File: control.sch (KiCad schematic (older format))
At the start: 3 parts, among them J4 ArduinoProMini

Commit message: Fix labels and lay resistors flat.
Left inputs to the line driver were backwards, because the datasheet had
an error. I think I "fixed"it before to match the datasheet.

I also decided to lay the resistors flat. They don't take up that much
room flat, and they will be easier to make pretty on the board, and more
stable with all the vibration.

Also updated the BOM and netlist.
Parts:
- R3: footprint Resistors_THT:R_Axial_DIN0204_L3.6mm_D1.6mm_P1.90mm_Vertical -> Resistors_THT:R_Axial_DIN0204_L3.6mm_D1.6mm_P5.08mm_Horizontal
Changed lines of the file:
@@
 F 0 "R3" V 4730 3400 50  0000 C CNN
 F 1 "330" V 4650 3400 50  0000 C CNN
-F 2 "Resistors_THT:R_Axial_DIN0204_L3.6mm_D1.6mm_P1.90mm_Vertical" V 4580 3400 50  0001 C CNN
+F 2 "Resistors_THT:R_Axial_DIN0204_L3.6mm_D1.6mm_P5.08mm_Horizontal" V 4580 3400 50  0001 C CNN
 F 3 "https://www.seielect.com/Catalog/SEI-CF_CFM.pdf" H 4650 3400 50  0001 C CNN
 	1    4650 3400

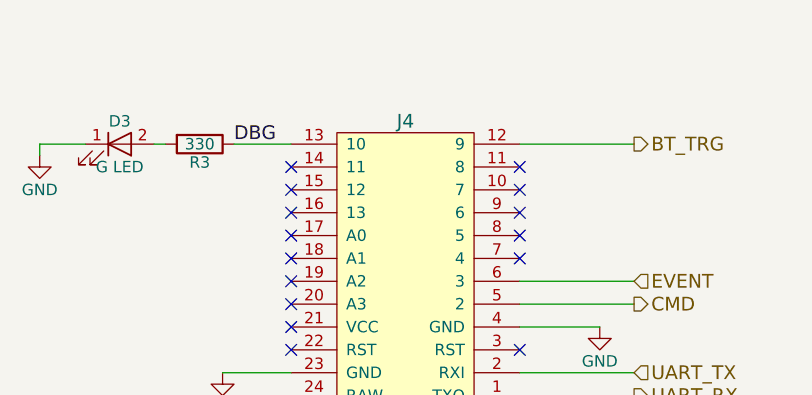
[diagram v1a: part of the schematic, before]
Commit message: Add a line in module and use a smaller jack.
Lots of changes:
Added a line in. This requires another audio switch, so that's added to
the audio switch module.
Also, since I'm using two jacks, I chose a smaller jack module. This
needed a new footprint, and a new 3d model. The footprint is trickier,
since it really needed slots, which OSH won't guarantee. I've given it a
unique footprint to try to optimize the pad size around the edges of the
pins.
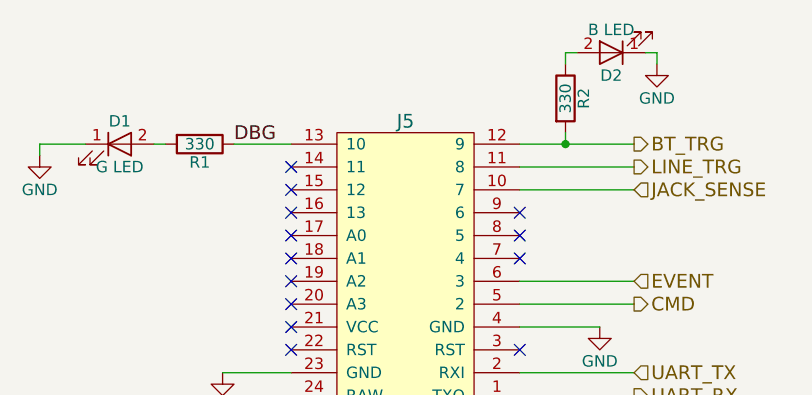
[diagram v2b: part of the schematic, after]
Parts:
- added D2: B LED, LEDs:LED_D3.0mm_Horizontal_O1.27mm_Z2.0mm, symbol LED
- added R2: 330, Resistors_THT:R_Axial_DIN0204_L3.6mm_D1.6mm_P5.08mm_Horizontal, symbol R
- renumbered D3 to D1, J4 to J5, R3 to R1
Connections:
- net BT_TRG: now also R2.2
- net GND: now also D2.1 (K)
- net JACK_SENSE: now reaches J5.10 (7)
- net LINE_TRG: now reaches J5.11 (8)
- new net: D2.2 (A), R2.1
- no-connect marks 15 -> 13
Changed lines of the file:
@@
 $Descr USLetter 11000 8500
 encoding utf-8
-Sheet 5 8
+Sheet 5 10
 Title "Blubaru"
 Date "2017-02-28"
@@
 $EndDescr
 $Comp
-L GND #PWR018
+L GND #PWR017
 U 1 1 589BF3A5
 P 6400 4200
-F 0 "#PWR018" H 6400 3950 50  0001 C CNN
+F 0 "#PWR017" H 6400 3950 50  0001 C CNN
 F 1 "GND" H 6400 4050 50  0000 C CNN
 F 2 "" H 6400 4200 50  0000 C CNN
@@
 $EndComp
 $Comp
-L GND #PWR019
+L GND #PWR018
 U 1 1 589BF4DD
 P 4750 4400
-F 0 "#PWR019" H 4750 4150 50  0001 C CNN
+F 0 "#PWR018" H 4750 4150 50  0001 C CNN
 F 1 "GND" H 4750 4250 50  0000 C CNN
 F 2 "" H 4750 4400 50  0000 C CNN
@@
 NoConn ~ 5050 4100
 NoConn ~ 5050 4300
-NoConn ~ 6050 3500
-NoConn ~ 6050 3600
 NoConn ~ 6050 3700
 NoConn ~ 6050 3800
@@
 	6050 4400 6550 4400
 $Comp
-L +12V #PWR020
+L +12V #PWR019
 U 1 1 58B175C7
 P 5050 4750
-F 0 "#PWR020" H 5050 4600 50  0001 C CNN
+F 0 "#PWR019" H 5050 4600 50  0001 C CNN
 F 1 "+12V" H 5050 4890 50  0000 C CNN
 F 2 "" H 5050 4750 50  0000 C CNN
@@
 NoConn ~ 6050 4300
 $Comp
-L LED D3
+L LED D1
 U 1 1 59385827
 P 4300 3400
-F 0 "D3" H 4300 3500 50  0000 C CNN
+F 0 "D1" H 4300 3500 50  0000 C CNN
 F 1 "G LED" H 4300 3300 50  0000 C CNN
 F 2 "LEDs:LED_D3.0mm_Horizontal_O1.27mm_Z2.0mm" H 4300 3400 50  0001 C CNN
@@
 $EndComp
 $Comp
-L R R3
+L R R1
 U 1 1 5939E4C5
 P 4650 3400
-F 0 "R3" V 4730 3400 50  0000 C CNN
+F 0 "R1" V 4730 3400 50  0000 C CNN
 F 1 "330" V 4650 3400 50  0000 C CNN
 F 2 "Resistors_THT:R_Axial_DIN0204_L3.6mm_D1.6mm_P5.08mm_Horizontal" V 4580 3400 50  0001 C CNN
@@
 $EndComp
 $Comp
-L GND #PWR021
+L GND #PWR020
 U 1 1 5939E808
 P 3950 3450
-F 0 "#PWR021" H 3950 3200 50  0001 C CNN
+F 0 "#PWR020" H 3950 3200 50  0001 C CNN
 F 1 "GND" H 3950 3300 50  0000 C CNN
 F 2 "" H 3950 3450 50  0001 C CNN
@@
 	3950 3400 3950 3450
 $Comp
-L ArduinoProMini J4
+L ArduinoProMini J5
 U 1 1 594DE4E8
 P 5550 4600
-F 0 "J4" H 5550 3300 60  0000 C CNN
+F 0 "J5" H 5550 3300 60  0000 C CNN
 F 1 "ArduinoProMini" H 5550 4600 60  0000 C CNN
 F 2 "blubaru:ProMicro" H 5550 4600 60  0001 C CNN
@@
 Text Label 4800 3400 0    60   ~ 0
 DBG
+Text HLabel 6550 3500 2    60   Output ~ 0
+LINE_TRG
+Wire Wire Line
+	6050 3500 6550 3500
+Text HLabel 6550 3600 2    60   Input ~ 0
+JACK_SENSE
+Wire Wire Line
+	6050 3600 6550 3600
+$Comp
+L R R2
+U 1 1 5975727A
+P 6250 3200
+F 0 "R2" V 6330 3200 50  0000 C CNN
+F 1 "330" V 6250 3200 50  0000 C CNN
+F 2 "Resistors_THT:R_Axial_DIN0204_L3.6mm_D1.6mm_P5.08mm_Horizontal" V 6180 3200 50  0001 C CNN
+F 3 "https://www.seielect.com/Catalog/SEI-CF_CFM.pdf" H 6250 3200 50  0001 C CNN
+	1    6250 3200
+	1    0    0    -1
+$EndComp
+$Comp
+L LED D2
+U 1 1 5975729B
+P 6450 3000
+F 0 "D2" H 6450 3100 50  0000 C CNN
+F 1 "B LED" H 6450 2900 50  0000 C CNN
+F 2 "LEDs:LED_D3.0mm_Horizontal_O1.27mm_Z2.0mm" H 6450 3000 50  0001 C CNN
+F 3 "http://www.kingbrightusa.com/images/catalog/SPEC/WP710A10LVBC-D.pdf" H 6450 3000 50  0001 C CNN
+	1    6450 3000
+	-1   0    0    1
+$EndComp
+$Comp
+L GND #PWR021
+U 1 1 597572DC
+P 6650 3050
+F 0 "#PWR021" H 6650 2800 50  0001 C CNN
+F 1 "GND" H 6650 2900 50  0000 C CNN
+F 2 "" H 6650 3050 50  0001 C CNN
+F 3 "" H 6650 3050 50  0001 C CNN
+	1    6650 3050
+	1    0    0    -1
+$EndComp
+Wire Wire Line
+	6650 3050 6650 3000
+Wire Wire Line
+	6650 3000 6600 3000
+Wire Wire Line
+	6300 3000 6250 3000
+Wire Wire Line
+	6250 3000 6250 3050
+Wire Wire Line
+	6250 3350 6250 3400
+Connection ~ 6250 3400
 $EndSCHEMATC

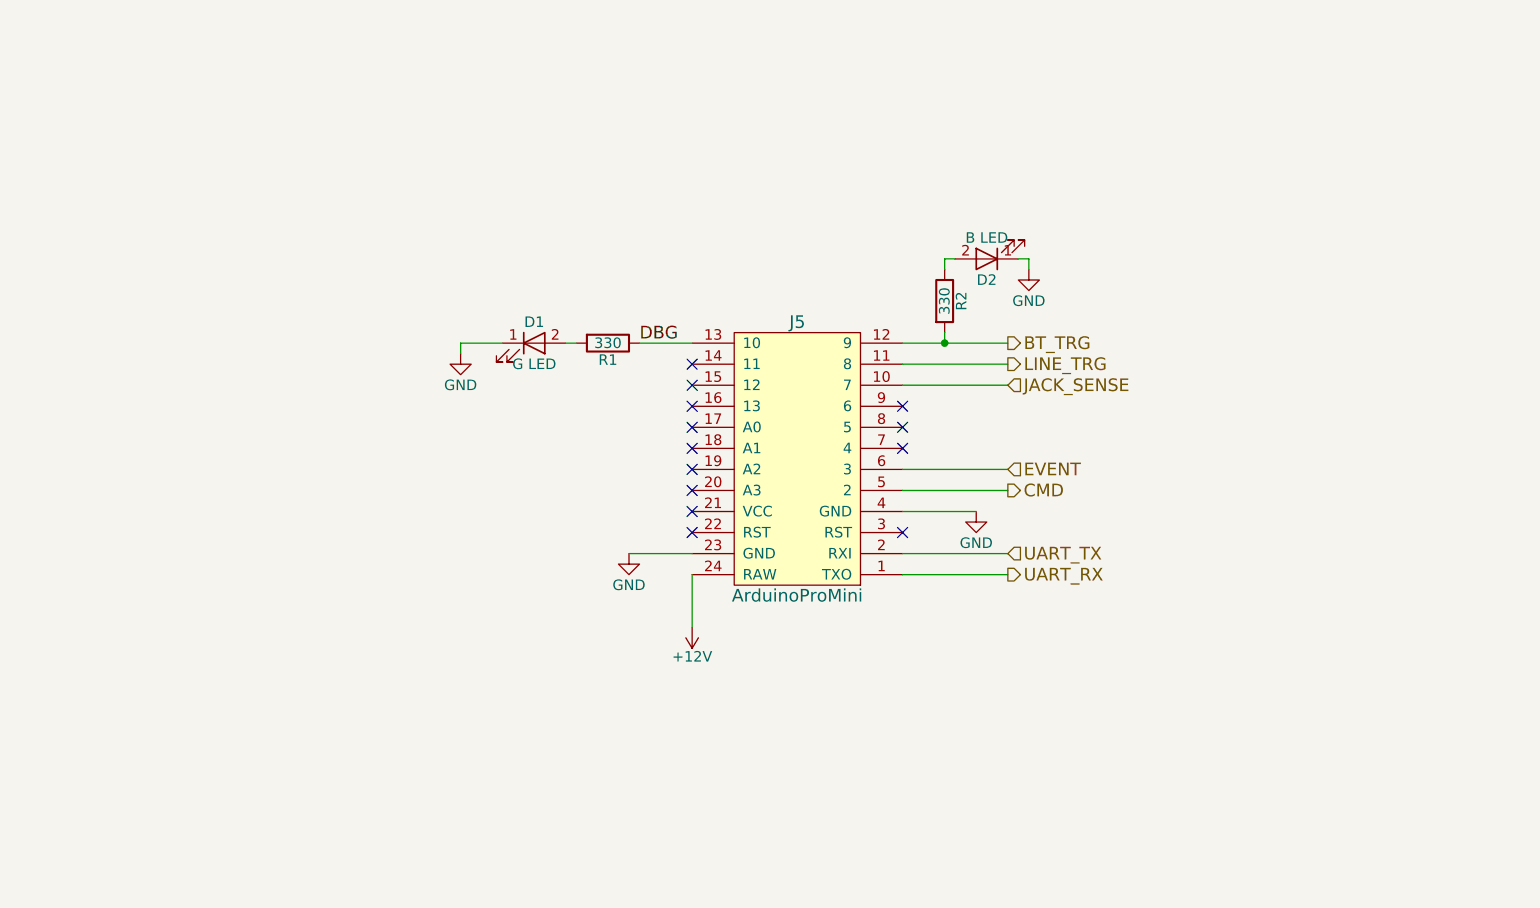
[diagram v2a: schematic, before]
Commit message: Major update to use Atmel ATTINY4313
Replace Pro Micro as microcontroller. Mostly contianed within the
control sheet.
Moved LEDs all onto control sheet.
Updated a few capacitors.
Added a reset switch. Still need to decide part.
Updated a few capacitor models for 4.0.7
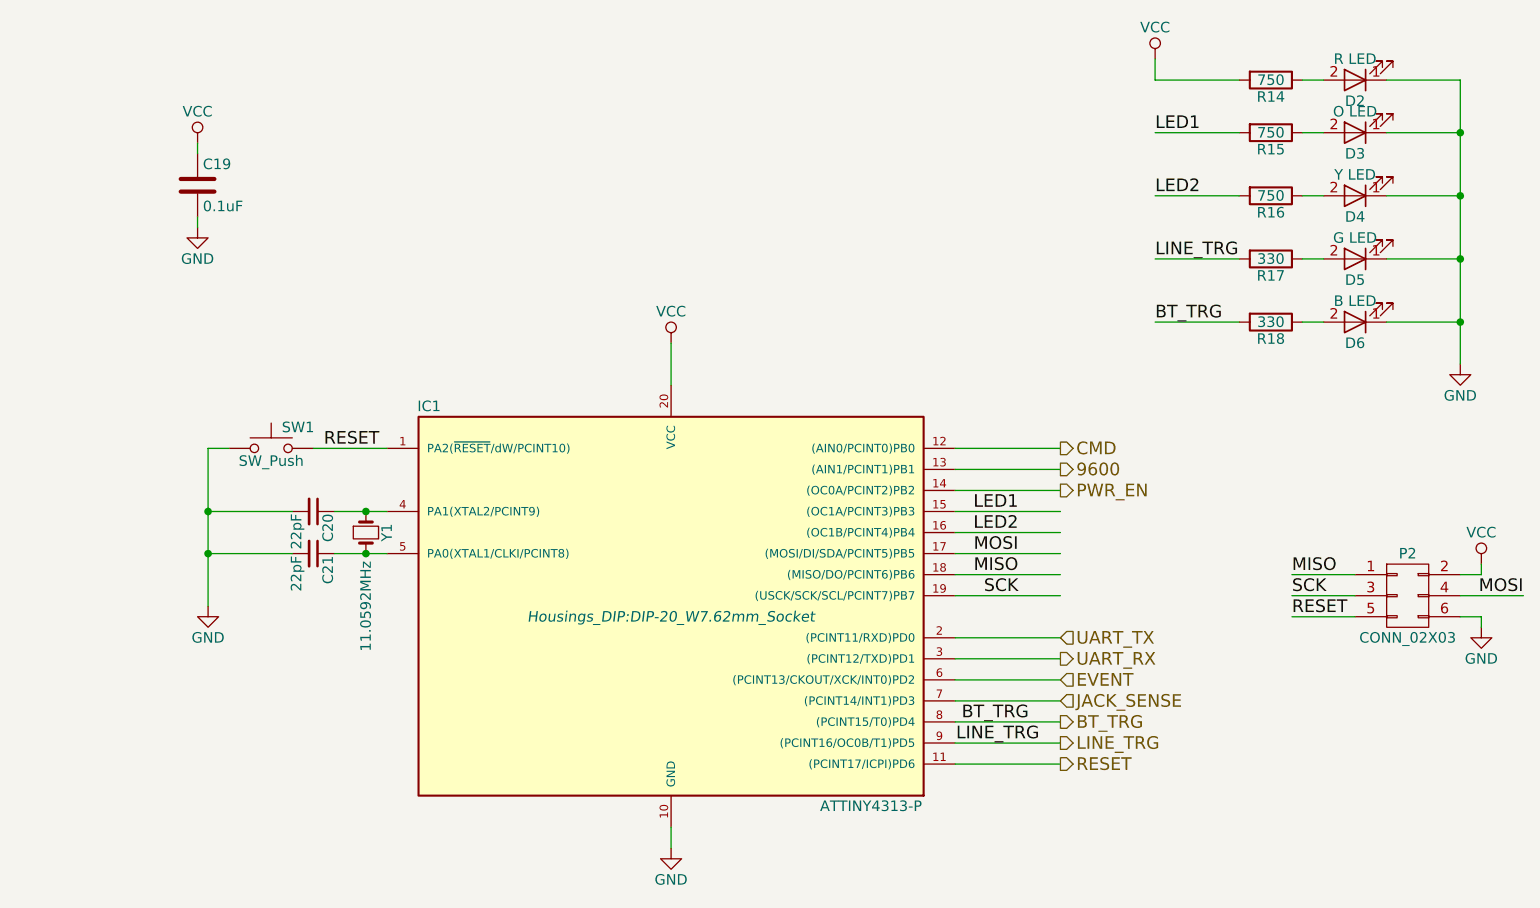
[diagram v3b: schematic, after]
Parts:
- removed J5: ArduinoProMini, blubaru:ProMicro, symbol ArduinoProMini
- added C19: 0.1uF, blubaru:C_Disc_D4.0mm_W2.6mm_P2.50mm, symbol C
- added C20, C21: 22pF, blubaru:C_Disc_D4.0mm_W2.6mm_P2.50mm, symbol C_Small
- added D2: R LED, LEDs:LED_D3.0mm_Horizontal_O1.27mm_Z2.0mm, symbol LED
- added D3: O LED, LEDs:LED_D3.0mm_Horizontal_O1.27mm_Z2.0mm, symbol LED
- added D6: B LED, LEDs:LED_D3.0mm_Horizontal_O1.27mm_Z2.0mm, symbol LED
- added IC1: ATTINY4313-P, Housings_DIP:DIP-20_W7.62mm_Socket, symbol ATTINY4313-P
- added P2: CONN_02X03, Pin_Headers:Pin_Header_Straight_2x03_Pitch2.54mm, symbol CONN_02X03
- added R14, R15: 750, Resistors_THT:R_Axial_DIN0204_L3.6mm_D1.6mm_P5.08mm_Horizontal, symbol R
- added R18: 330, Resistors_THT:R_Axial_DIN0204_L3.6mm_D1.6mm_P5.08mm_Horizontal, symbol R
- added SW1: SW_Push, Buttons_Switches_THT:SW_Tactile_SPST_Angled_PTS645Vx58-2LFS, symbol SW_Push
- added Y1: 11.0592MHz, Crystals:Crystal_HC49-4H_Vertical, symbol Crystal_Small
- D4: renamed from D1; value G LED -> Y LED
- D5: renamed from D2; value B LED -> G LED
- R16: renamed from R1; value 330 -> 750
- renumbered R2 to R17
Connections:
- net labels added: 9600, LED1, LED2, MISO, MOSI, PWR_EN, RESET, SCK, VCC
- net labels removed: +12V, DBG
- wire segments 19 -> 51
- no-connect marks 13 -> 0
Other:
- moved on the sheet: D4, D5, R16, R17
